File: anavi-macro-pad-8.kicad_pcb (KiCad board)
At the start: 2 copper layers, 135 x 47.1 mm, 50 parts, among them J1 USB_B_Micro, J3 Conn_01x03_Male, J4 Conn_01x03_Male, Q1 BC817, SW1 SW_DIP_x01, SW2 SW_DIP_x01, SW3 SW_DIP_x01, SW4 SW_DIP_x01, SW5 SW_DIP_x01, SW6 SW_DIP_x01, SW7 SW_DIP_x01, SW8 SW_DIP_x01, U1 ATmega32U4-AU, Y1 Crystal

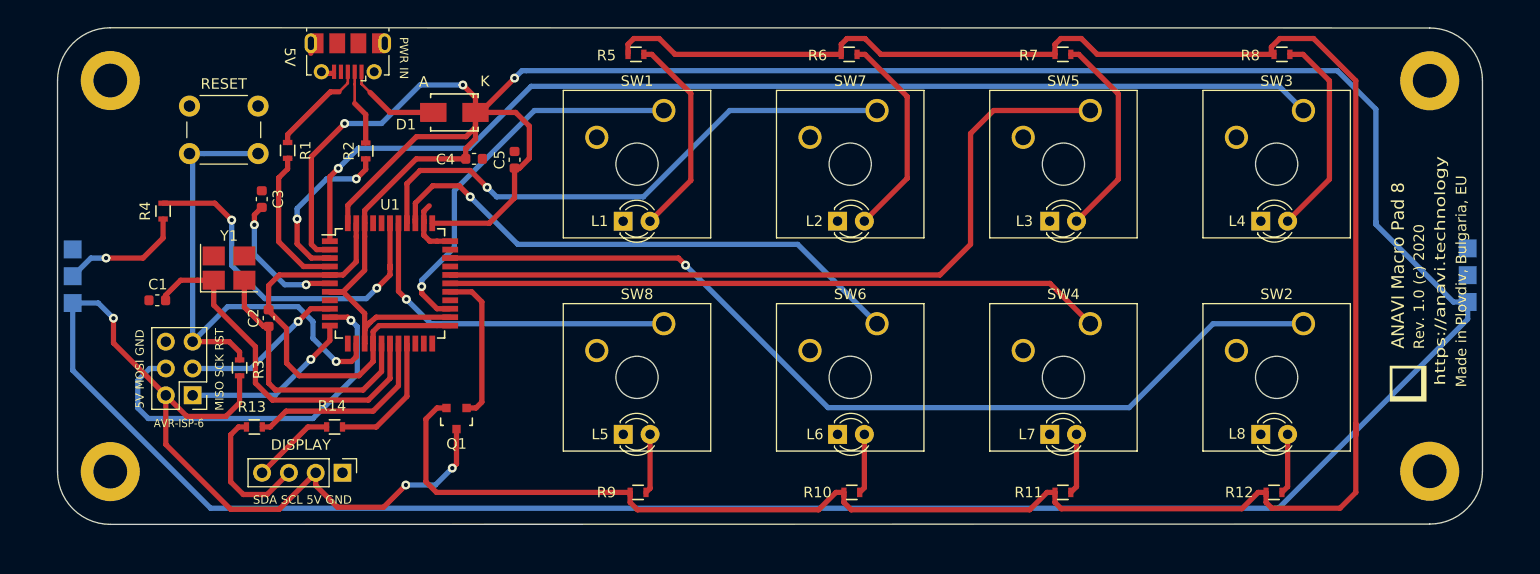
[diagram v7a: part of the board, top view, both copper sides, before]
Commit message: anavi-macro-pad-8: Improvements
Rotate headers to match the direction of the addressable LED
strip, update labels.

Signed-off-by: Leon Anavi <leon@anavi.org>
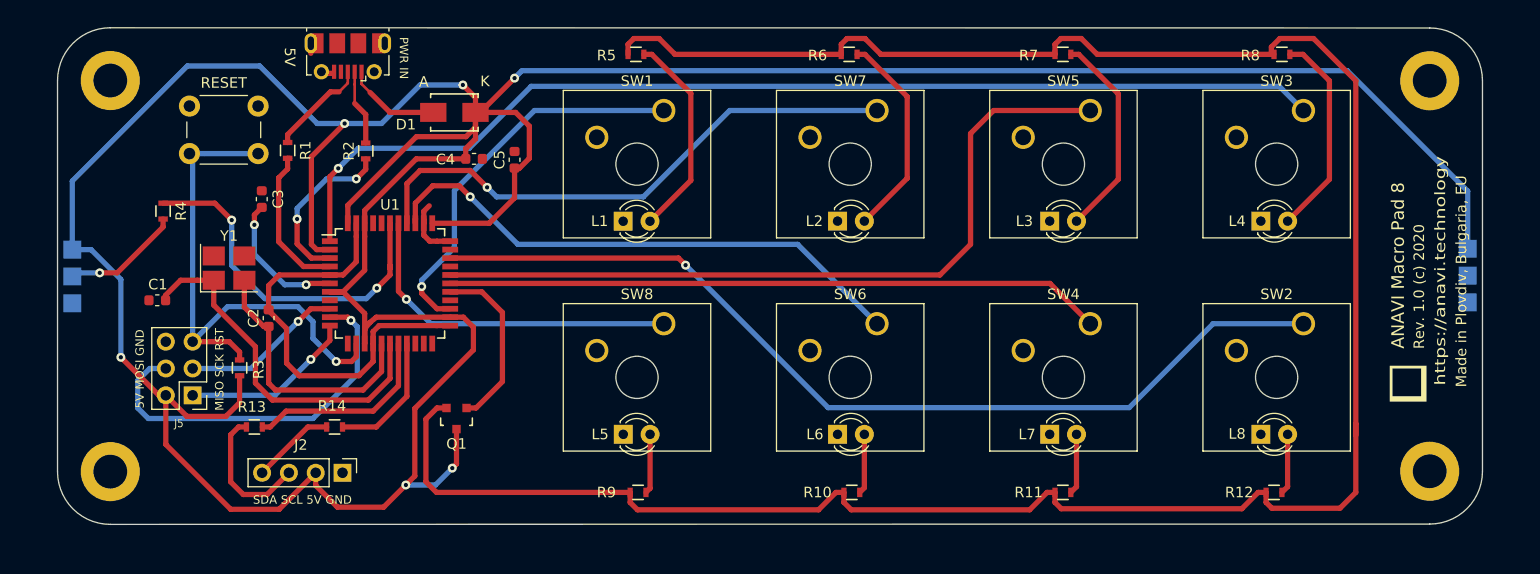
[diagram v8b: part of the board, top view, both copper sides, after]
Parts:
- Q1: value BC817 -> Q_NPN_BEC
- moved J3 5.06 mm to (46.4, 76.0), turned to 180 degrees
- moved J4 5.04 mm to (178.6, 75.9), turned to 180 degrees
- renumbered DISPLAY to J2, AVR-ISP-6 to J5
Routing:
- net +5V: track 448.4 -> 354.3 mm
- net /BACKLIT: track 14.6 -> 16.7 mm
- net Net-(J3-Pad2): track 11.9 -> 11.3 mm
